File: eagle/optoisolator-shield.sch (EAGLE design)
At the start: 48 parts, among them Q1 NPN, Q2 NPN, Q3 NPN, Q4 NPN, Q5 NPN, Q6 NPN, U1 OPTO, U2 OPTO, U3 OPTO

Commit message: added cam and util directories; routed board, touch-ups still in progress
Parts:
- JP1, JP8: value (none) -> M03_3.5MM
- JP10, JP9: value M023.5MM -> M02_3.5MM
- R1, R10, R11, R12, R13, R14, R15, R16, R17, R18, R2, R3, R4, R5, R6, R7, R8, R9: device SparkFun:RESISTOR0402 -> SparkFun-Passives:RESISTOR0603-RES
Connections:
- net !ADC_RESET_1 renamed N$601
- removed net AGND: JP4.35, JP4.36, SPI1.6
- removed net IN6: OUTPUT2.10, OUTPUT2.12, OUTPUT2.14, OUTPUT2.16, OUTPUT2.2, OUTPUT2.4, OUTPUT2.6, OUTPUT2.8
- new net GND1: SPI1.6
- new net N$602: JP4.35, JP4.36
- net OPTO_IN6: now also OUTPUT2.10, OUTPUT2.12, OUTPUT2.14, OUTPUT2.16, OUTPUT2.2, OUTPUT2.4, OUTPUT2.6, OUTPUT2.8
- net OUT5: now also JP9.2
- net OUT6: now also JP10.2
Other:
- moved on the sheet: R1, R13, R15, R3, R7, R9

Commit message: updated board silkscreen to include instructions
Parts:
- renumbered INPUT1 to INPUT1B, INPUT2 to INPUT2B, INPUT3 to INPUT1C, INPUT4 to INPUT2C, OUTPUT1 to 1A, OUTPUT2 to 2A
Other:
- note added: "Output"
- note added: "Released under a Creative Commons By-Attribution Share-Alike 4.0 license"
- note removed: "Released under a Creative Commons By-Attribution Share-Alike 3.0 license"

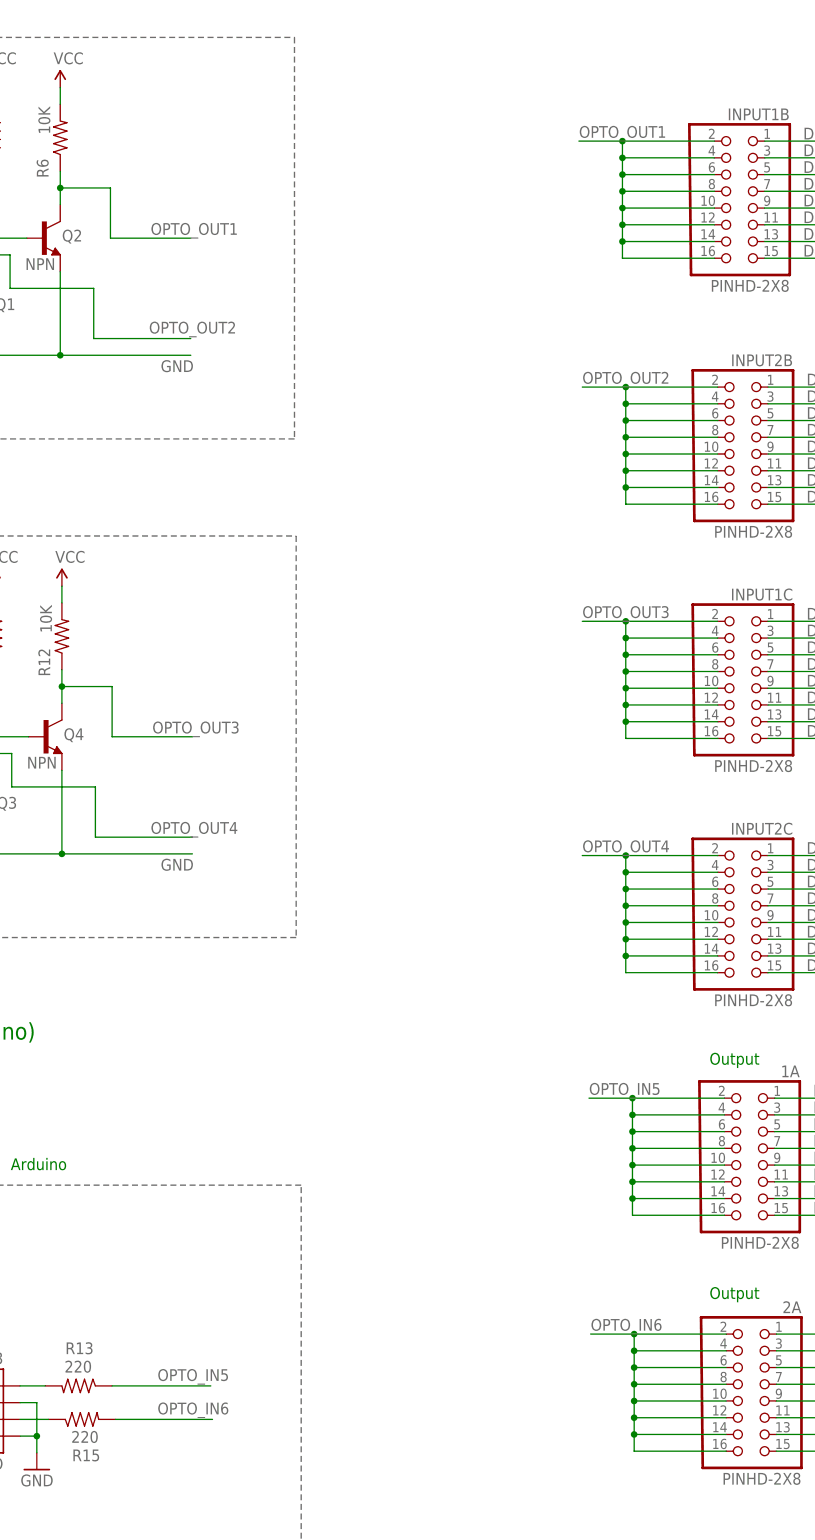
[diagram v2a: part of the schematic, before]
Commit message: updated signal names for optoisolator in/out to match the board silkscreen labels
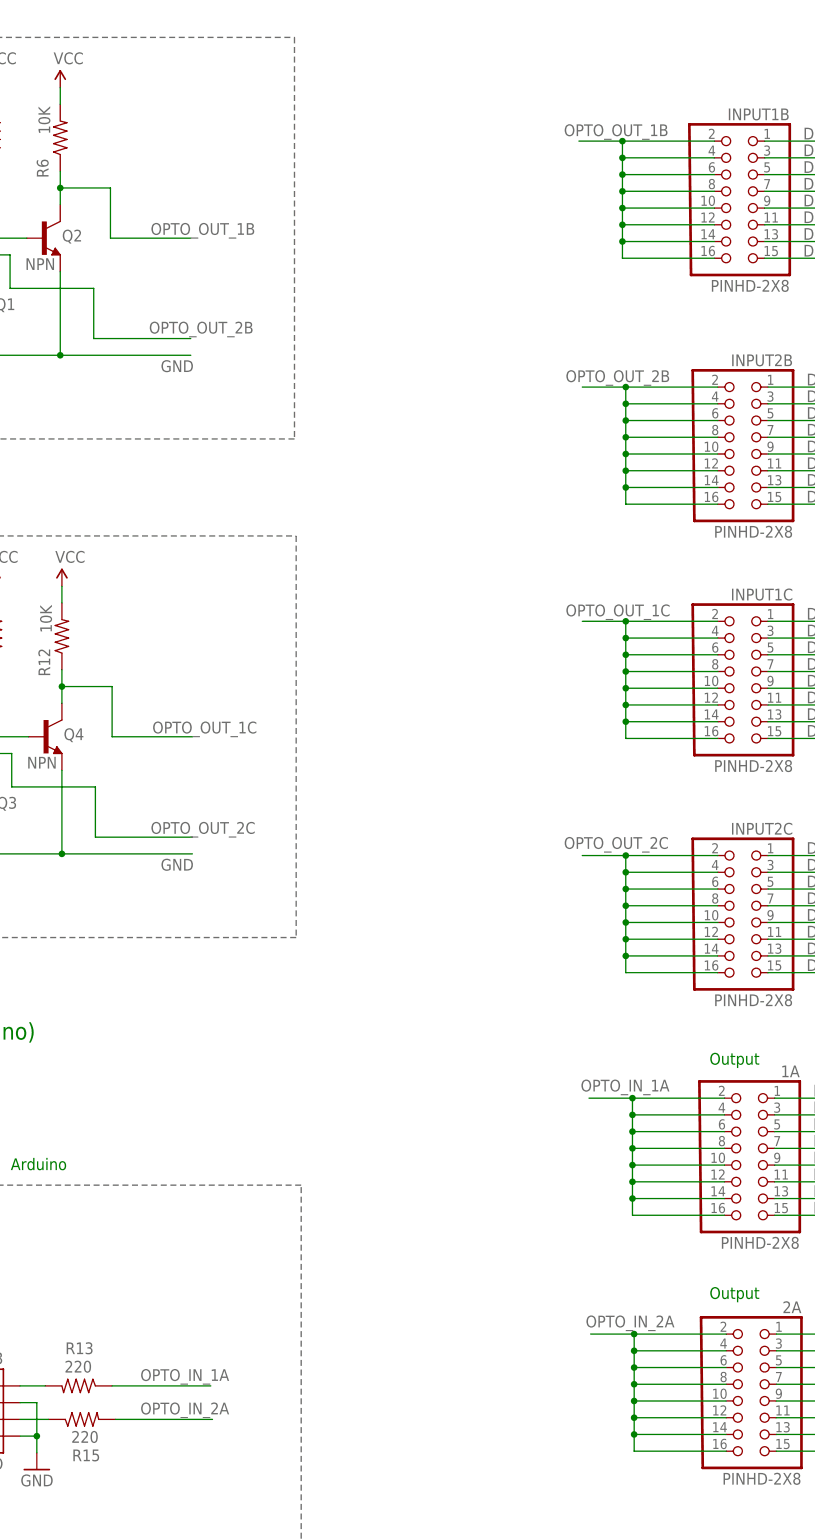
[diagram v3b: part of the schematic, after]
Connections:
- net OPTO_IN5 renamed OPTO_IN_1A
- net OPTO_IN6 renamed OPTO_IN_2A
- net OPTO_OUT1 renamed OPTO_OUT_1B
- net OPTO_OUT2 renamed OPTO_OUT_2B
- net OPTO_OUT3 renamed OPTO_OUT_1C
- net OPTO_OUT4 renamed OPTO_OUT_2C
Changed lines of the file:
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@@
 </segment>
 </net>
-<net name="OPTO_OUT1" class="0">
+<net name="OPTO_OUT_1B" class="0">
 <segment>
 <wire x1="107.188" y1="244.856" x2="107.188" y2="242.316" width="0.1524" layer="91"/>
@@
 <wire x1="192.532" y1="249.428" x2="185.928" y2="249.428" width="0.1524" layer="91"/>
 <junction x="192.532" y="249.428"/>
-<label x="185.928" y="249.936" size="1.778" layer="95"/>
-</segment>
-</net>
-<net name="OPTO_OUT2" class="0">
+<label x="183.642" y="250.19" size="1.778" layer="95"/>
+</segment>
+</net>
+<net name="OPTO_OUT_2B" class="0">
 <segment>
 <wire x1="97.028" y1="229.616" x2="97.028" y2="232.156" width="0.1524" layer="91"/>
@@
 <wire x1="193.04" y1="212.09" x2="186.436" y2="212.09" width="0.1524" layer="91"/>
 <junction x="193.04" y="212.09"/>
-<label x="186.436" y="212.598" size="1.778" layer="95"/>
-</segment>
-</net>
-<net name="OPTO_OUT3" class="0">
+<label x="183.896" y="212.852" size="1.778" layer="95"/>
+</segment>
+</net>
+<net name="OPTO_OUT_1C" class="0">
 <segment>
 <wire x1="107.442" y1="169.164" x2="107.442" y2="166.624" width="0.1524" layer="91"/>
@@
 <wire x1="193.04" y1="176.53" x2="186.436" y2="176.53" width="0.1524" layer="91"/>
 <junction x="193.04" y="176.53"/>
-<label x="186.436" y="177.038" size="1.778" layer="95"/>
-</segment>
-</net>
-<net name="OPTO_OUT4" class="0">
+<label x="183.896" y="177.292" size="1.778" layer="95"/>
+</segment>
+</net>
+<net name="OPTO_OUT_2C" class="0">
 <segment>
 <wire x1="97.282" y1="153.924" x2="97.282" y2="156.464" width="0.1524" layer="91"/>
@@
 <wire x1="193.04" y1="140.97" x2="186.436" y2="140.97" width="0.1524" layer="91"/>
 <junction x="193.04" y="140.97"/>
-<label x="186.436" y="141.478" size="1.778" layer="95"/>
-</segment>
-</net>
-<net name="OPTO_IN5" class="0">
+<label x="183.642" y="141.986" size="1.778" layer="95"/>
+</segment>
+</net>
+<net name="OPTO_IN_1A" class="0">
 <segment>
 <wire x1="115.062" y1="60.452" x2="130.048" y2="60.452" width="0.1524" layer="91"/>
@@
 <wire x1="194.056" y1="104.14" x2="187.452" y2="104.14" width="0.1524" layer="91"/>
 <junction x="194.056" y="104.14"/>
-<label x="187.452" y="104.648" size="1.778" layer="95"/>
-</segment>
-</net>
-<net name="OPTO_IN6" class="0">
+<label x="186.182" y="105.156" size="1.778" layer="95"/>
+</segment>
+</net>
+<net name="OPTO_IN_2A" class="0">
 <segment>
 <wire x1="130.302" y1="55.372" x2="115.57" y2="55.372" width="0.1524" layer="91"/>
@@
 <wire x1="194.31" y1="68.326" x2="187.706" y2="68.326" width="0.1524" layer="91"/>
 <junction x="194.31" y="68.326"/>
-<label x="187.706" y="68.834" size="1.778" layer="95"/>
-</segment>
-</net>
+<label x="186.944" y="69.342" size="1.778" layer="95"/>
+</segment>
+</net>

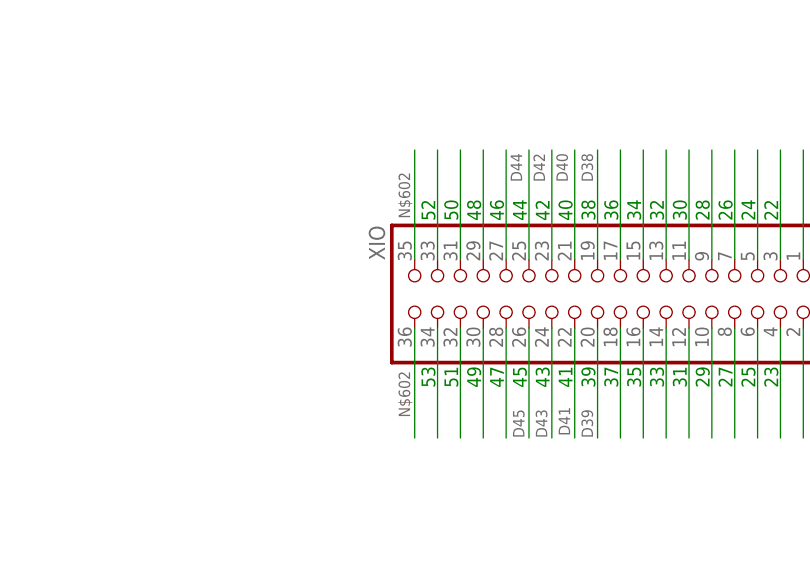
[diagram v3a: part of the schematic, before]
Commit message: fixed XIO orientation error propagated from HackEEG shield
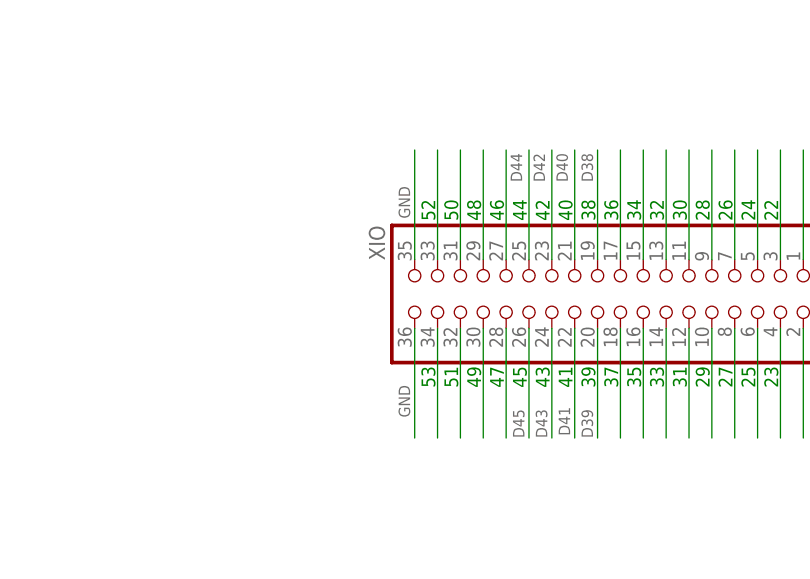
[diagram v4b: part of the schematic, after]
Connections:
- removed net N$602: JP4.35, JP4.36
- net GND: now also JP4.35, JP4.36
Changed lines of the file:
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@@
-</segment>
-</net>
-<net name="N$602" class="0">
-<segment>
-<pinref part="JP4" gate="A" pin="35"/>
-<wire x1="312.166" y1="124.968" x2="312.166" y2="137.16" width="0.1524" layer="91"/>
-<label x="311.658" y="129.54" size="1.27" layer="95" rot="R90"/>
-</segment>
-<segment>
-<pinref part="JP4" gate="A" pin="36"/>
-<wire x1="312.166" y1="117.348" x2="312.166" y2="105.156" width="0.1524" layer="91"/>
-<label x="311.658" y="107.442" size="1.27" layer="95" rot="R90"/>
 </segment>
 </net>
@@
 <label x="279.146" y="235.458" size="1.778" layer="95"/>
 </segment>
-</net>
+<segment>
+<pinref part="JP4" gate="A" pin="35"/>
+<wire x1="312.166" y1="124.968" x2="312.166" y2="137.16" width="0.1524" layer="91"/>
+<label x="311.658" y="129.54" size="1.27" layer="95" rot="R90"/>
+</segment>
+<segment>
+<pinref part="JP4" gate="A" pin="36"/>
+<wire x1="312.166" y1="117.348" x2="312.166" y2="105.156" width="0.1524" layer="91"/>
+<label x="311.658" y="107.442" size="1.27" layer="95" rot="R90"/>
+</segment>
+</net>

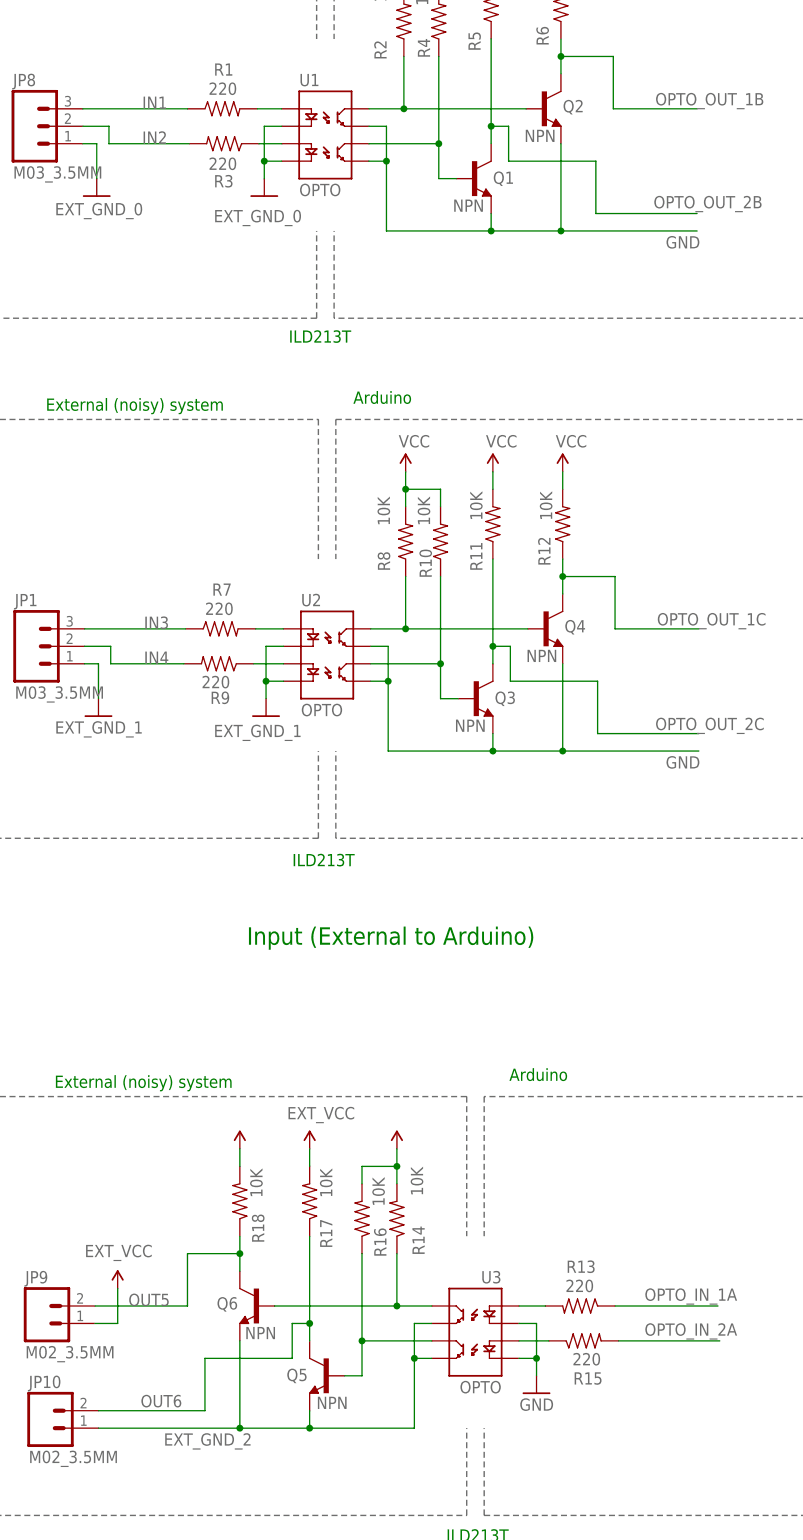
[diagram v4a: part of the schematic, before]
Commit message: updated silkscreen with correct dac0/1 and canrx/tx labels; updated fiducials so 2 share the same X and 2 share the same Y coordinates
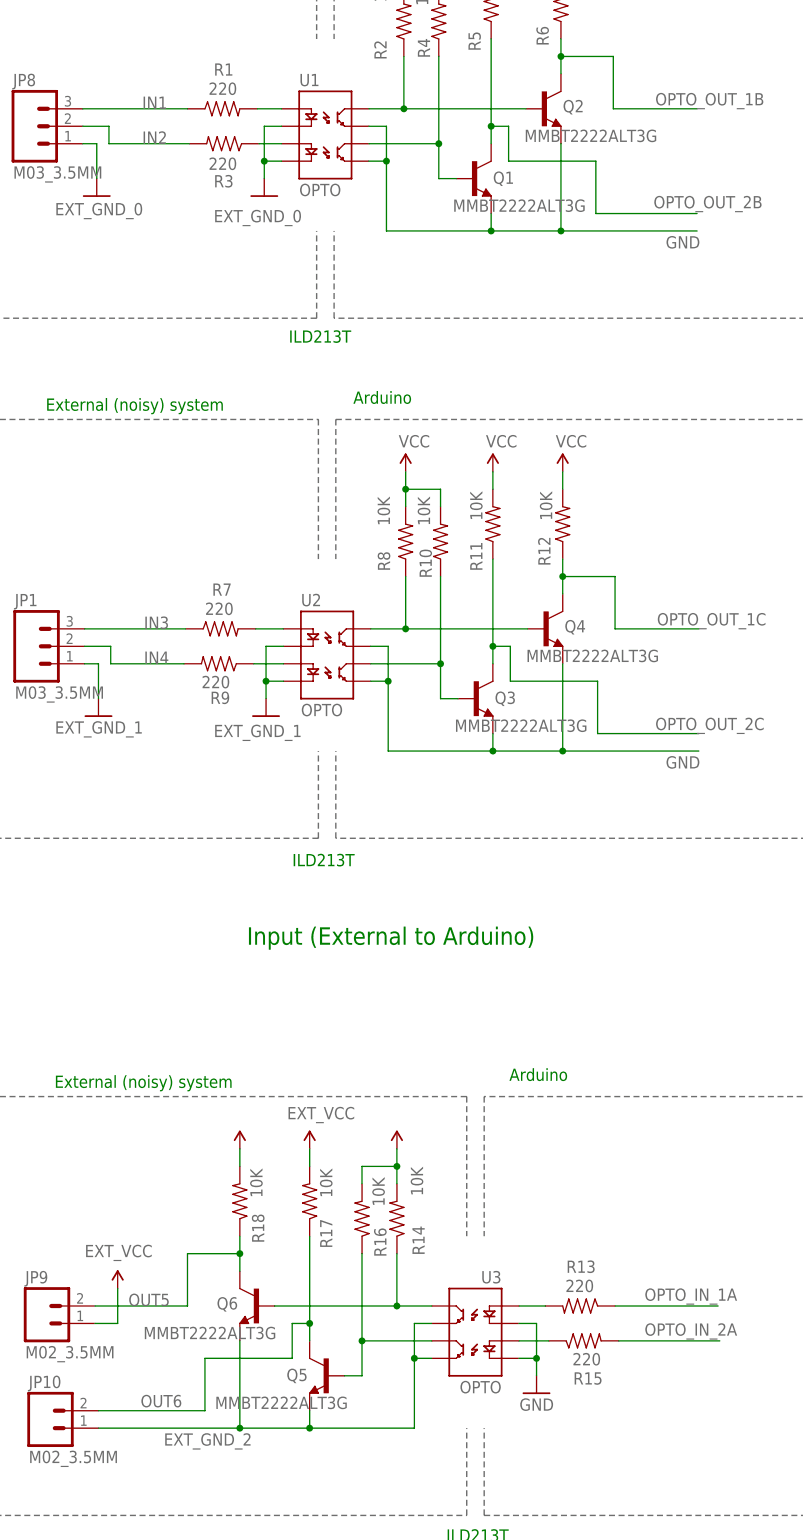
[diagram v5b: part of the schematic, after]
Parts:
- Q1, Q2, Q3, Q4, Q5, Q6: value NPN -> MMBT2222ALT3G
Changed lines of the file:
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@@
 <part name="R10" library="SparkFun-Passives" deviceset="RESISTOR" device="0603-RES" value="10K"/>
 <part name="GND3" library="SparkFun" deviceset="GND" device="" value="EXT_GND_1"/>
-<part name="Q3" library="SparkFun" deviceset="TRANSISTOR_NPN" device="SOT23-3" value="NPN"/>
+<part name="Q3" library="SparkFun" deviceset="TRANSISTOR_NPN" device="SOT23-3" value="MMBT2222ALT3G"/>
 <part name="P+7" library="SparkFun" deviceset="VCC" device="" value="VCC"/>
 <part name="R11" library="SparkFun-Passives" deviceset="RESISTOR" device="0603-RES" value="10K"/>
-<part name="Q4" library="SparkFun" deviceset="TRANSISTOR_NPN" device="SOT23-3" value="NPN"/>
+<part name="Q4" library="SparkFun" deviceset="TRANSISTOR_NPN" device="SOT23-3" value="MMBT2222ALT3G"/>
 <part name="R12" library="SparkFun-Passives" deviceset="RESISTOR" device="0603-RES" value="10K"/>
 <part name="P+8" library="SparkFun" deviceset="VCC" device="" value="VCC"/>
@@
 <part name="R4" library="SparkFun-Passives" deviceset="RESISTOR" device="0603-RES" value="10K"/>
 <part name="GND4" library="SparkFun" deviceset="GND" device="" value="EXT_GND_0"/>
-<part name="Q1" library="SparkFun" deviceset="TRANSISTOR_NPN" device="SOT23-3" value="NPN"/>
+<part name="Q1" library="SparkFun" deviceset="TRANSISTOR_NPN" device="SOT23-3" value="MMBT2222ALT3G"/>
 <part name="P+3" library="SparkFun" deviceset="VCC" device="" value="VCC"/>
 <part name="R5" library="SparkFun-Passives" deviceset="RESISTOR" device="0603-RES" value="10K"/>
-<part name="Q2" library="SparkFun" deviceset="TRANSISTOR_NPN" device="SOT23-3" value="NPN"/>
+<part name="Q2" library="SparkFun" deviceset="TRANSISTOR_NPN" device="SOT23-3" value="MMBT2222ALT3G"/>
 <part name="R6" library="SparkFun-Passives" deviceset="RESISTOR" device="0603-RES" value="10K"/>
 <part name="P+4" library="SparkFun" deviceset="VCC" device="" value="VCC"/>
@@
 <part name="R16" library="SparkFun-Passives" deviceset="RESISTOR" device="0603-RES" value="10K"/>
 <part name="P+10" library="SparkFun" deviceset="VCC" device="" value="EXT_VCC"/>
-<part name="Q5" library="SparkFun" deviceset="TRANSISTOR_NPN" device="SOT23-3" value="NPN"/>
+<part name="Q5" library="SparkFun" deviceset="TRANSISTOR_NPN" device="SOT23-3" value="MMBT2222ALT3G"/>
 <part name="P+11" library="SparkFun" deviceset="VCC" device="" value="EXTERNAL_VCC"/>
 <part name="R17" library="SparkFun-Passives" deviceset="RESISTOR" device="0603-RES" value="10K"/>
-<part name="Q6" library="SparkFun" deviceset="TRANSISTOR_NPN" device="SOT23-3" value="NPN"/>
+<part name="Q6" library="SparkFun" deviceset="TRANSISTOR_NPN" device="SOT23-3" value="MMBT2222ALT3G"/>
 <part name="R18" library="SparkFun-Passives" deviceset="RESISTOR" device="0603-RES" value="10K"/>
 <part name="P+12" library="SparkFun" deviceset="VCC" device="" value="EXTERNAL_VCC"/>
